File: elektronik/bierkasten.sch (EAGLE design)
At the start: 72 parts, among them Q1 BC547B

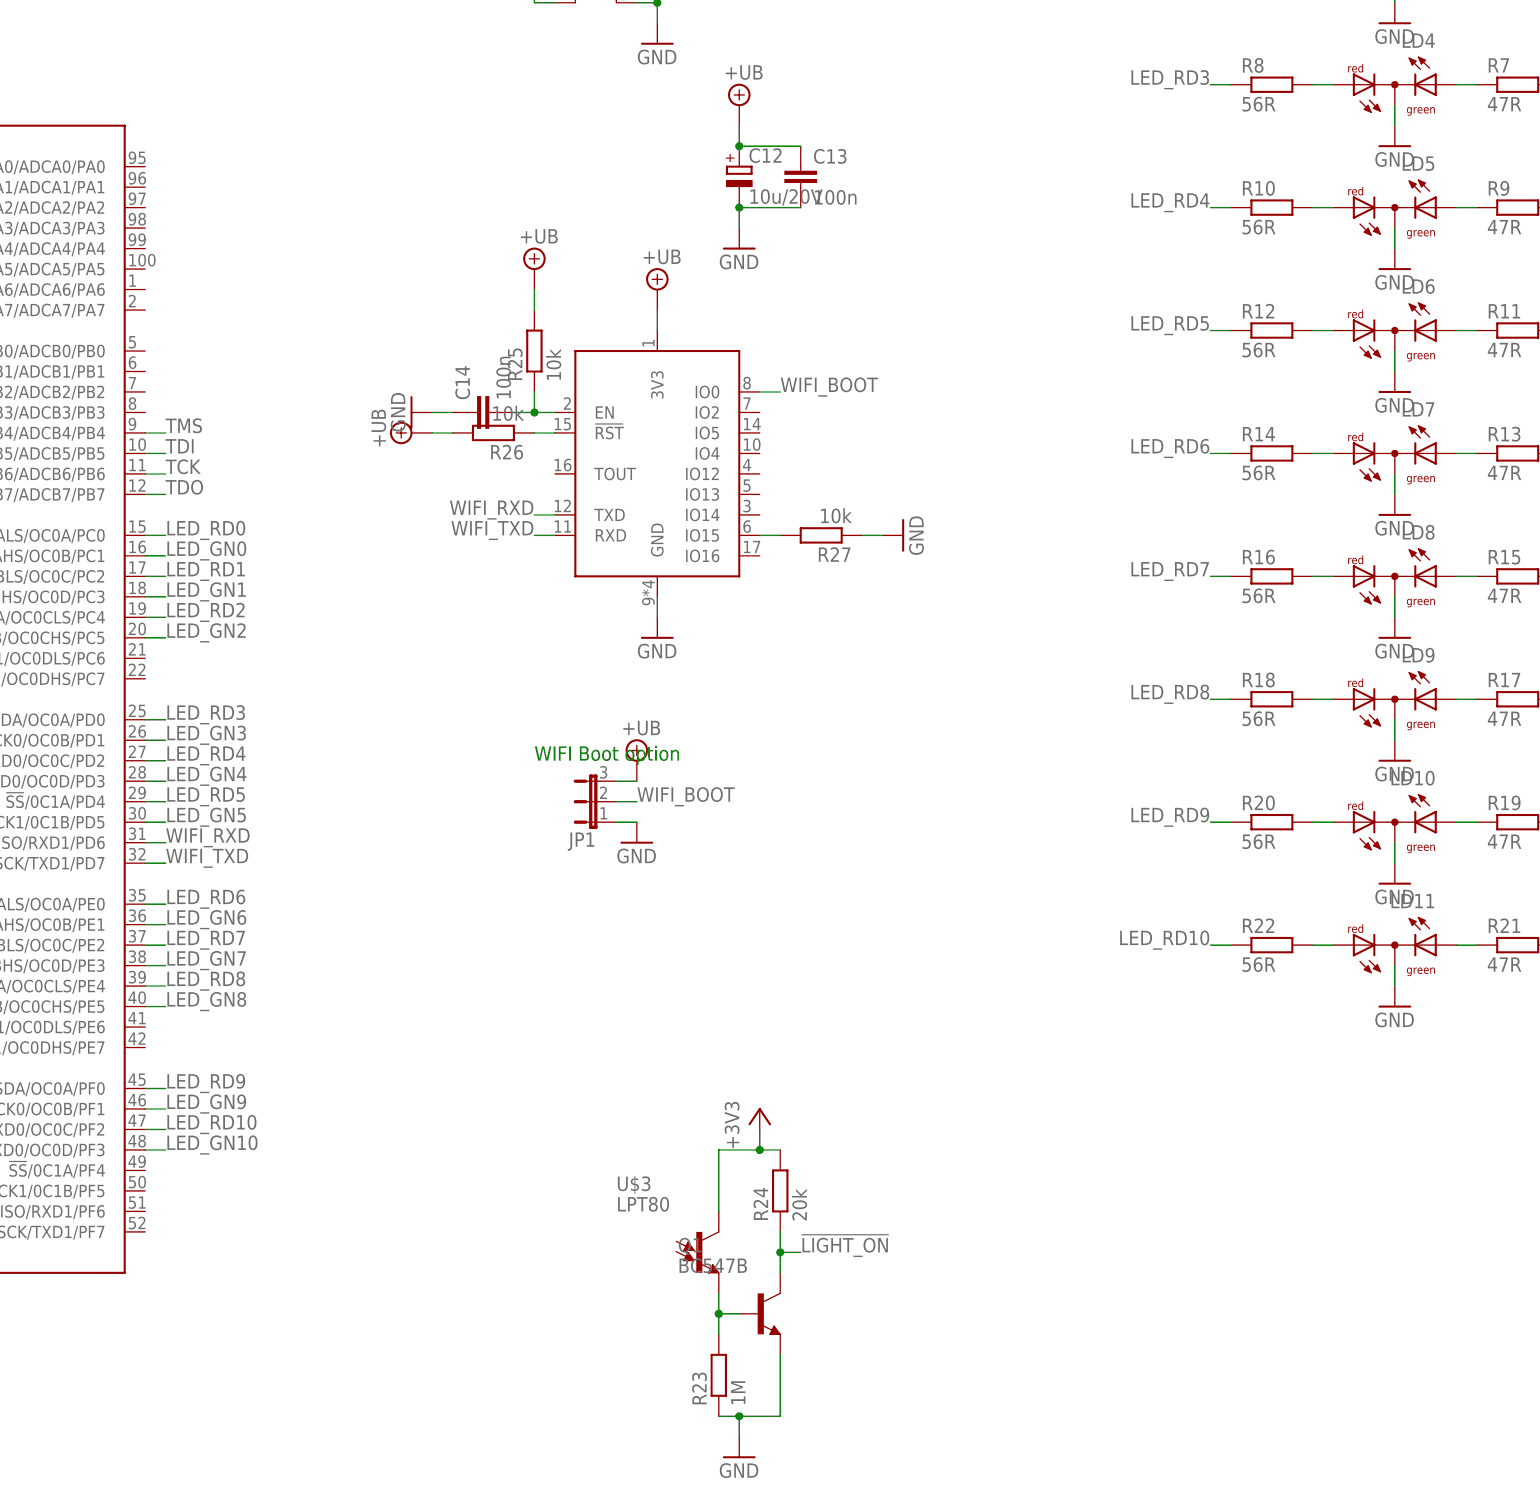
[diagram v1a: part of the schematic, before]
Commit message: Stecker für User-Wahlschalter hinzugefügt.
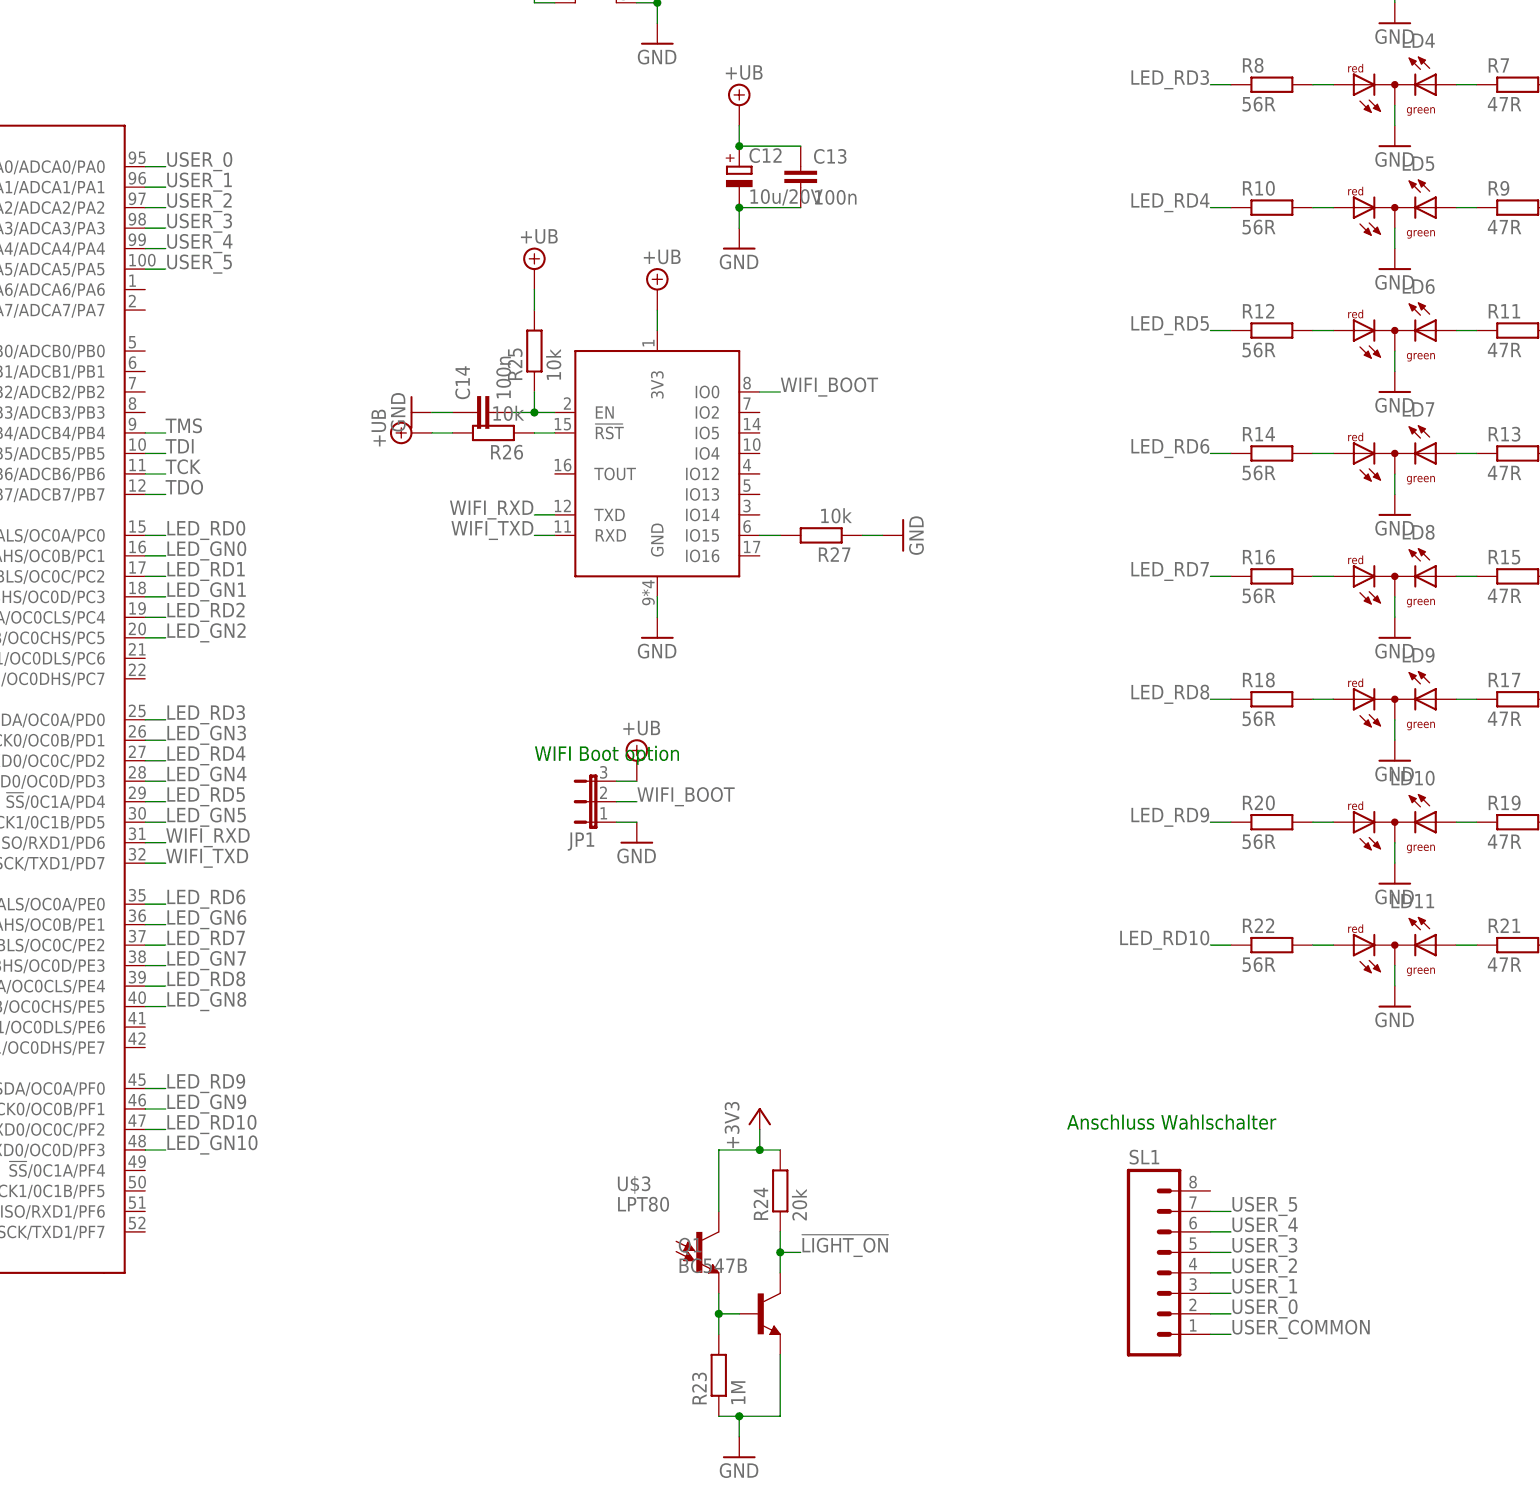
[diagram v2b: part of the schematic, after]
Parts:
- added SL1: (no value), con-amp-quick:M08
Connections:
- new net USER_0: SL1.2, U$1.AREFA/ADA0/ADCA0/PA0
- new net USER_1: SL1.3, U$1.ACA1/ADCA1/PA1
- new net USER_2: SL1.4, U$1.DACA0/ACA2/ADCA2/PA2
- new net USER_3: SL1.5, U$1.DACA1/ACA3/ADCA3/PA3
- new net USER_4: SL1.6, U$1.ACA4/ADCA4/PA4
- new net USER_5: SL1.7, U$1.ACA5/ADCA5/PA5
- new net USER_COMMON: SL1.1
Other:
- note added: "Anschluss Wahlschalter"
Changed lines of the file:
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@@
 <attribute name="REICHELT" value="SL 1X36G 2,54:JUMPER 2,54 GN*10"/>
 </part>
+<part name="SL1" library="con-amp-quick" library_urn="urn:adsk.eagle:library:125" deviceset="M08" device="" package3d_urn="urn:adsk.eagle:package:5962/1"/>
 </parts>
 <sheets>
@@
 <text x="86.36" y="20.32" size="1.778" layer="91">Libraries available on https://github.com/Stenkelfled/EAGLE-stuff.git</text>
 <text x="129.54" y="116.84" size="1.778" layer="91">WIFI Boot option</text>
+<text x="195.58" y="71.12" size="1.778" layer="91">Anschluss Wahlschalter</text>
 </plain>
 <instances>
@@
 <attribute name="REICHELT" x="96.52" y="10.16" size="1.778" layer="96" display="off"/>
 </instance>
+<instance part="SL1" gate="G$1" x="208.28" y="53.34"/>
 </instances>
 <busses>
@@
 </segment>
 </net>
+<net name="USER_5" class="0">
+<segment>
+<pinref part="SL1" gate="G$1" pin="7"/>
+<wire x1="213.36" y1="60.96" x2="215.9" y2="60.96" width="0.1524" layer="91"/>
+<label x="215.9" y="60.96" size="1.778" layer="95"/>
+</segment>
+<segment>
+<pinref part="U$1" gate="G$1" pin="ACA5/ADCA5/PA5"/>
+<wire x1="81.28" y1="177.8" x2="83.82" y2="177.8" width="0.1524" layer="91"/>
+<label x="83.82" y="177.8" size="1.778" layer="95"/>
+</segment>
+</net>
+<net name="USER_4" class="0">
+<segment>
+<pinref part="SL1" gate="G$1" pin="6"/>
+<wire x1="213.36" y1="58.42" x2="215.9" y2="58.42" width="0.1524" layer="91"/>
+<label x="215.9" y="58.42" size="1.778" layer="95"/>
+</segment>
+<segment>
+<pinref part="U$1" gate="G$1" pin="ACA4/ADCA4/PA4"/>
+<wire x1="81.28" y1="180.34" x2="83.82" y2="180.34" width="0.1524" layer="91"/>
+<label x="83.82" y="180.34" size="1.778" layer="95"/>
+</segment>
+</net>
+<net name="USER_3" class="0">
+<segment>
+<pinref part="SL1" gate="G$1" pin="5"/>
+<wire x1="213.36" y1="55.88" x2="215.9" y2="55.88" width="0.1524" layer="91"/>
+<label x="215.9" y="55.88" size="1.778" layer="95"/>
+</segment>
+<segment>
+<pinref part="U$1" gate="G$1" pin="DACA1/ACA3/ADCA3/PA3"/>
+<wire x1="81.28" y1="182.88" x2="83.82" y2="182.88" width="0.1524" layer="91"/>
+<label x="83.82" y="182.88" size="1.778" layer="95"/>
+</segment>
+</net>
+<net name="USER_2" class="0">
+<segment>
+<pinref part="SL1" gate="G$1" pin="4"/>
+<wire x1="213.36" y1="53.34" x2="215.9" y2="53.34" width="0.1524" layer="91"/>
+<label x="215.9" y="53.34" size="1.778" layer="95"/>
+</segment>
+<segment>
+<pinref part="U$1" gate="G$1" pin="DACA0/ACA2/ADCA2/PA2"/>
+<wire x1="81.28" y1="185.42" x2="83.82" y2="185.42" width="0.1524" layer="91"/>
+<label x="83.82" y="185.42" size="1.778" layer="95"/>
+</segment>
+</net>
+<net name="USER_1" class="0">
+<segment>
+<pinref part="SL1" gate="G$1" pin="3"/>
+<wire x1="213.36" y1="50.8" x2="215.9" y2="50.8" width="0.1524" layer="91"/>
+<label x="215.9" y="50.8" size="1.778" layer="95"/>
+</segment>
+<segment>
+<pinref part="U$1" gate="G$1" pin="ACA1/ADCA1/PA1"/>
+<wire x1="81.28" y1="187.96" x2="83.82" y2="187.96" width="0.1524" layer="91"/>
+<label x="83.82" y="187.96" size="1.778" layer="95"/>
+</segment>
+</net>
+<net name="USER_0" class="0">
+<segment>
+<pinref part="SL1" gate="G$1" pin="2"/>
+<wire x1="213.36" y1="48.26" x2="215.9" y2="48.26" width="0.1524" layer="91"/>
+<label x="215.9" y="48.26" size="1.778" layer="95"/>
+</segment>
+<segment>
+<pinref part="U$1" gate="G$1" pin="AREFA/ADA0/ADCA0/PA0"/>
+<wire x1="81.28" y1="190.5" x2="83.82" y2="190.5" width="0.1524" layer="91"/>
+<label x="83.82" y="190.5" size="1.778" layer="95"/>
+</segment>
+</net>
+<net name="USER_COMMON" class="0">
+<segment>
+<pinref part="SL1" gate="G$1" pin="1"/>
+<wire x1="213.36" y1="45.72" x2="215.9" y2="45.72" width="0.1524" layer="91"/>
+<label x="215.9" y="45.72" size="1.778" layer="95"/>
+</segment>
+</net>

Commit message: Schaltplan fertig
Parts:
- added C15: 100n, rcl_STE:C-EUC0603
- added C16: 10u/20V, rcl:CPOL-EUB/3528-21W
- added Q2: NXP2301P-SOT23, mosfet_STE:NXP2301P-SOT23
- added R28: 10k, rcl:R-EU_R0603
- added SL2: (no value), con-amp-quick:M02
- added U$16: NCP1117ST33T3G, power_STE:NCP1117ST33
- C1, C10, C13, C14, C2, C3, C4, C5, C6, C7, C8, C9: FARNELL 432210 -> (none); REICHELT X7R-G0603 100N -> (none)
- C11, C12: REICHELT TAJ 3528 10/20 -> (none)
- FERRITE1: REICHELT BLM21PG 331 -> (none)
- LD1, LD10, LD11, LD2, LD3, LD4, LD5, LD6, LD7, LD8, LD9: REICHELT LED 5 RG-3 -> (none)
- Q1: REICHELT BC 547B -> (none)
- R1, R11, R13, R15, R17, R19, R21, R3, R5, R7, R9: FARNELL 2502461 -> (none); REICHELT RND 0603 1 47 -> (none)
- R10, R12, R14, R16, R18, R2, R20, R22, R4, R6, R8: REICHELT RND 0603 1 56 -> (none)
- R23: REICHELT RND 0603 1 1,0M -> (none)
- R24: REICHELT RND 0603 1 20K -> (none)
- R25, R26, R27: FARNELL 2502397 -> (none); REICHELT RND 0603 1 10K -> (none)
- TA1: FARNELL 2292960 -> (none)
- U$1: REICHELT ATXMEGA 128A1-AU -> (none)
- U$10, U$11, U$12, U$13, U$14, U$4, U$5, U$6, U$7, U$8, U$9: value SWITCH_SINGLE-WIRED -> ESE11HS2; REICHELT ESE 11HS2 -> (none)
- U$2: REICHELT WSL 10G -> (none)
- U$3: REICHELT LPT 80 -> (none)
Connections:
- removed net USER_COMMON: SL1.1
- new net BATTERY: SL2.2, U$16.IN
- new net WIFI_ENABLE: Q2.G, R28.1, U$1.ACA0OUT/ACA7/ADCA7/PA7
- net +3V3: now also C15.1, C16.+, Q2.S, R28.2, SL1.1, U$16.OUT
- net +UB: now also Q2.D
- net GND: now also C15.2, C16.-, SL2.1, U$16.GND
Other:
- note added: "Batterie"
- note added: "nochmal kontrollieren, ob der richtig rum ist..."
- moved on the sheet: TA1

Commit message: Layout fertig
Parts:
- added C17: 100n, rcl_STE:C-EUC0603
- added C18: 10u/20V, rcl:CPOL-EUB/3528-21W
- C1, C10, C13, C14, C15, C2, C3, C4, C5, C6, C7, C8, C9: FARNELL (none) -> 432210; REICHELT (none) -> X7R-G0603 100N
- C11, C12, C16: REICHELT (none) -> TAJ 3528 10/20
- FERRITE1: REICHELT (none) -> BLM21PG 331
- LD1, LD10, LD11, LD2, LD3, LD4, LD5, LD6, LD7, LD8, LD9: REICHELT (none) -> LED 5 RG-3
- Q1: REICHELT (none) -> BC 547B
- Q2: REICHELT (none) -> NX2301P NXP
- R1, R11, R13, R15, R17, R19, R21, R3, R5, R7, R9: FARNELL (none) -> 2502461; REICHELT (none) -> RND 0603 1 47
- R10, R12, R14, R16, R18, R2, R20, R22, R4, R6, R8: REICHELT (none) -> RND 0603 1 56
- R23: REICHELT (none) -> RND 0603 1 1,0M
- R24: REICHELT (none) -> RND 0603 1 20K
- R25, R26, R27, R28: FARNELL (none) -> 2502397; REICHELT (none) -> RND 0603 1 10K
- SL1: REICHELT (none) -> PSS 254/8G:PSK 254/8W
- SL2: REICHELT (none) -> PSS 254/2G:PSK 254/2W
- TA1: FARNELL (none) -> 2292960; REICHELT (none) -> Taster 9314; WUERTH (none) -> 430 182 043 816
- U$1: REICHELT (none) -> ATXMEGA 128A1-AU
- U$10, U$11, U$12, U$13, U$14, U$4, U$5, U$6, U$7, U$8, U$9: REICHELT (none) -> ESE 11HS2
- U$16: REICHELT (none) -> NCP 1117 ST33T3G
- U$17: REICHELT SL 1X36G 2,54:JUMPER 2,54 GN*10 -> SL 1X36G 2,54:JUMPER 2,54 GN*10:HALTER 4XUM3-1DK:CLIP 9V
- U$2: REICHELT (none) -> WSL 10G
- U$3: REICHELT (none) -> LPT 80
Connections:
- net BATTERY: now also C17.1, C18.+
- net GND: now also C17.2, C18.-
- net WIFI_ENABLE: now also U$1.PK6/SDRAM; no longer U$1.ACA0OUT/ACA7/ADCA7/PA7
